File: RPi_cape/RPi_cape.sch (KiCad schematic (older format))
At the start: 108 parts, among them J1 Conn_01x04, J10 Conn_01x02, J11 Conn_01x02, J12 Conn_01x02, J16 Conn_01x06, J2 Conn_01x02, J3 Conn_01x02, J4 Conn_01x02, J5 Conn_01x03, J6 Conn_01x03, J7 Conn_01x02, J8 Conn_02x20_Odd_Even, J9 Conn_01x02, U1 TL431A, U2 ADC128D818, U3 ADC128D818

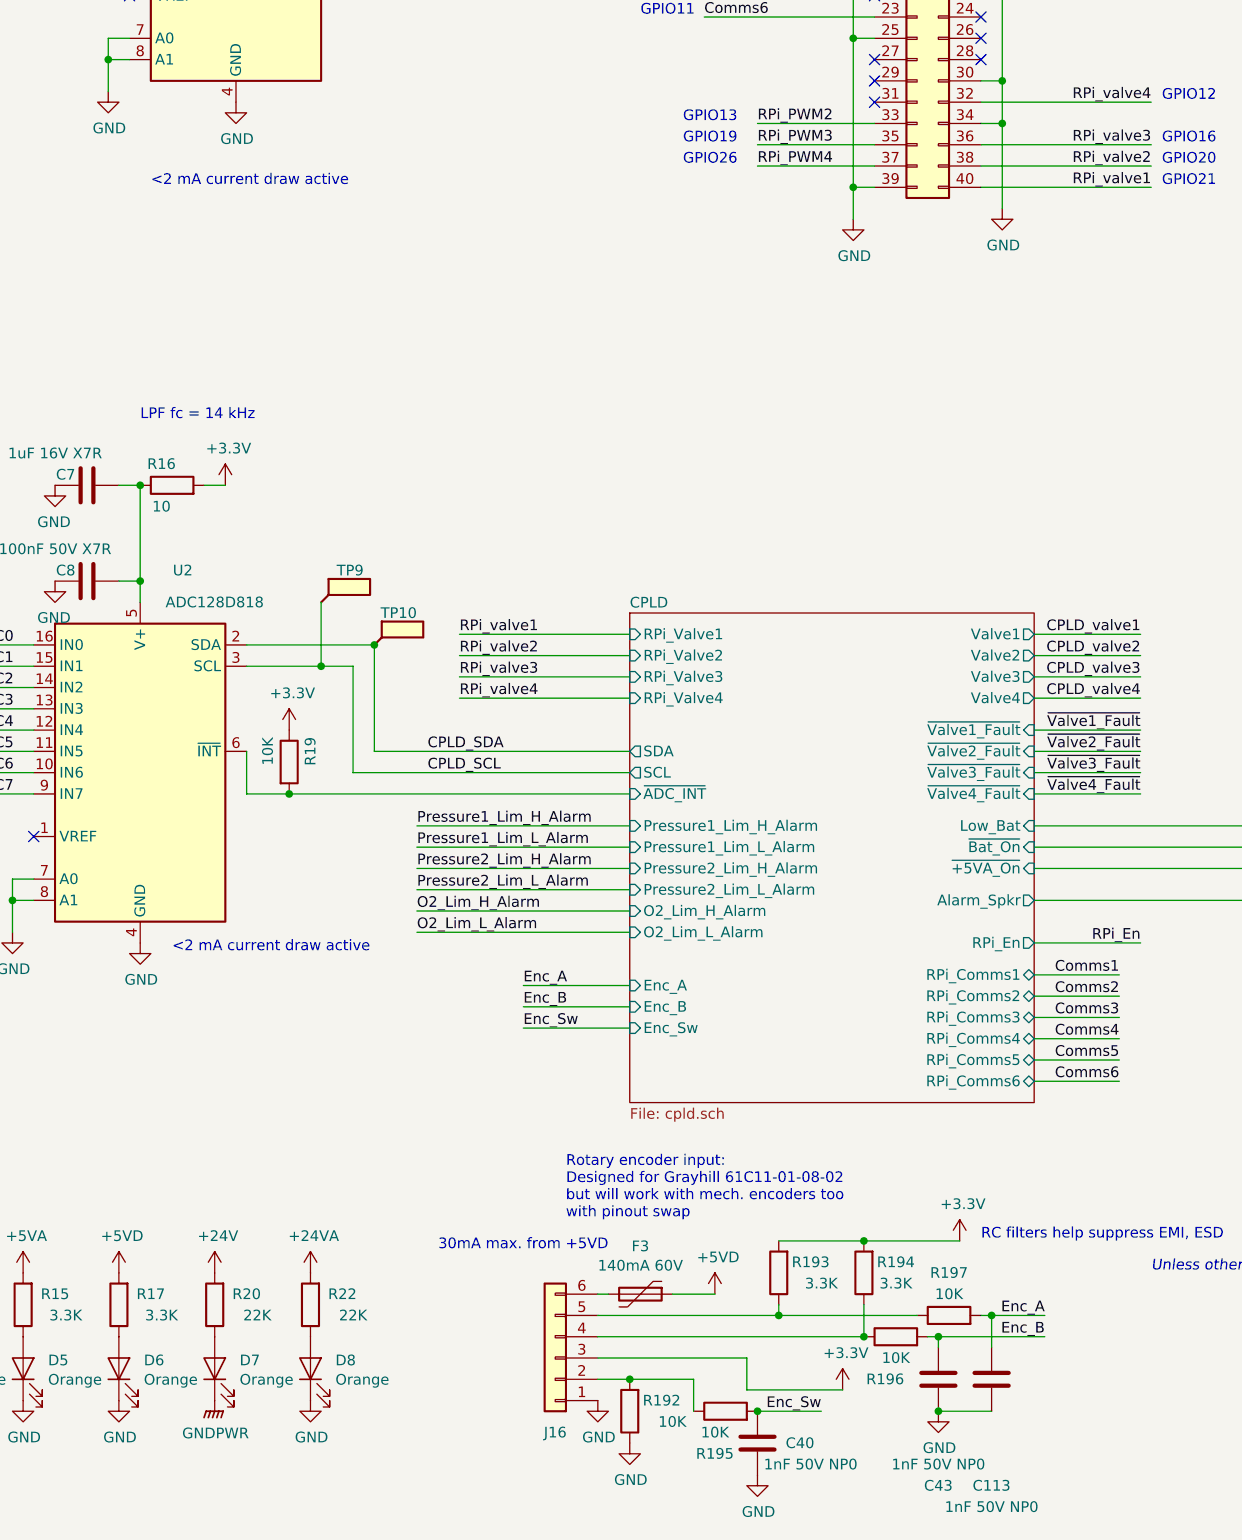
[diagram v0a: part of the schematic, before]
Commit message: Analog upgrades and extra encoder connectors
Renamed a few files
Removed "costing BOM" as difficult to keep up to date, easy to regenerate
Toughened under-voltage detect circuits by adding hysteresis to +5V detect for +BATT diode-OR (R236), filtering to power-down alarm detect input (C85)
Added connector options (J15, J21) for Grayhill C14-series rotary encoder with cable
Changed R190 from 3K to 2.4K to increase overhead on base current required for saturation, and consolidate BOM
Added 3 solderable testpoints for expanding CPLD pin options (TP44-46), adjusted some CPLD pin assignments to allow physical routing to pins
Fixed valve motion detector by changing comparator's hysteresis to AC-only, changing NPN's series resistor to 1K (allows low-enough DC level to count as logic low), and adding optional filtering cap C115 to offset divider
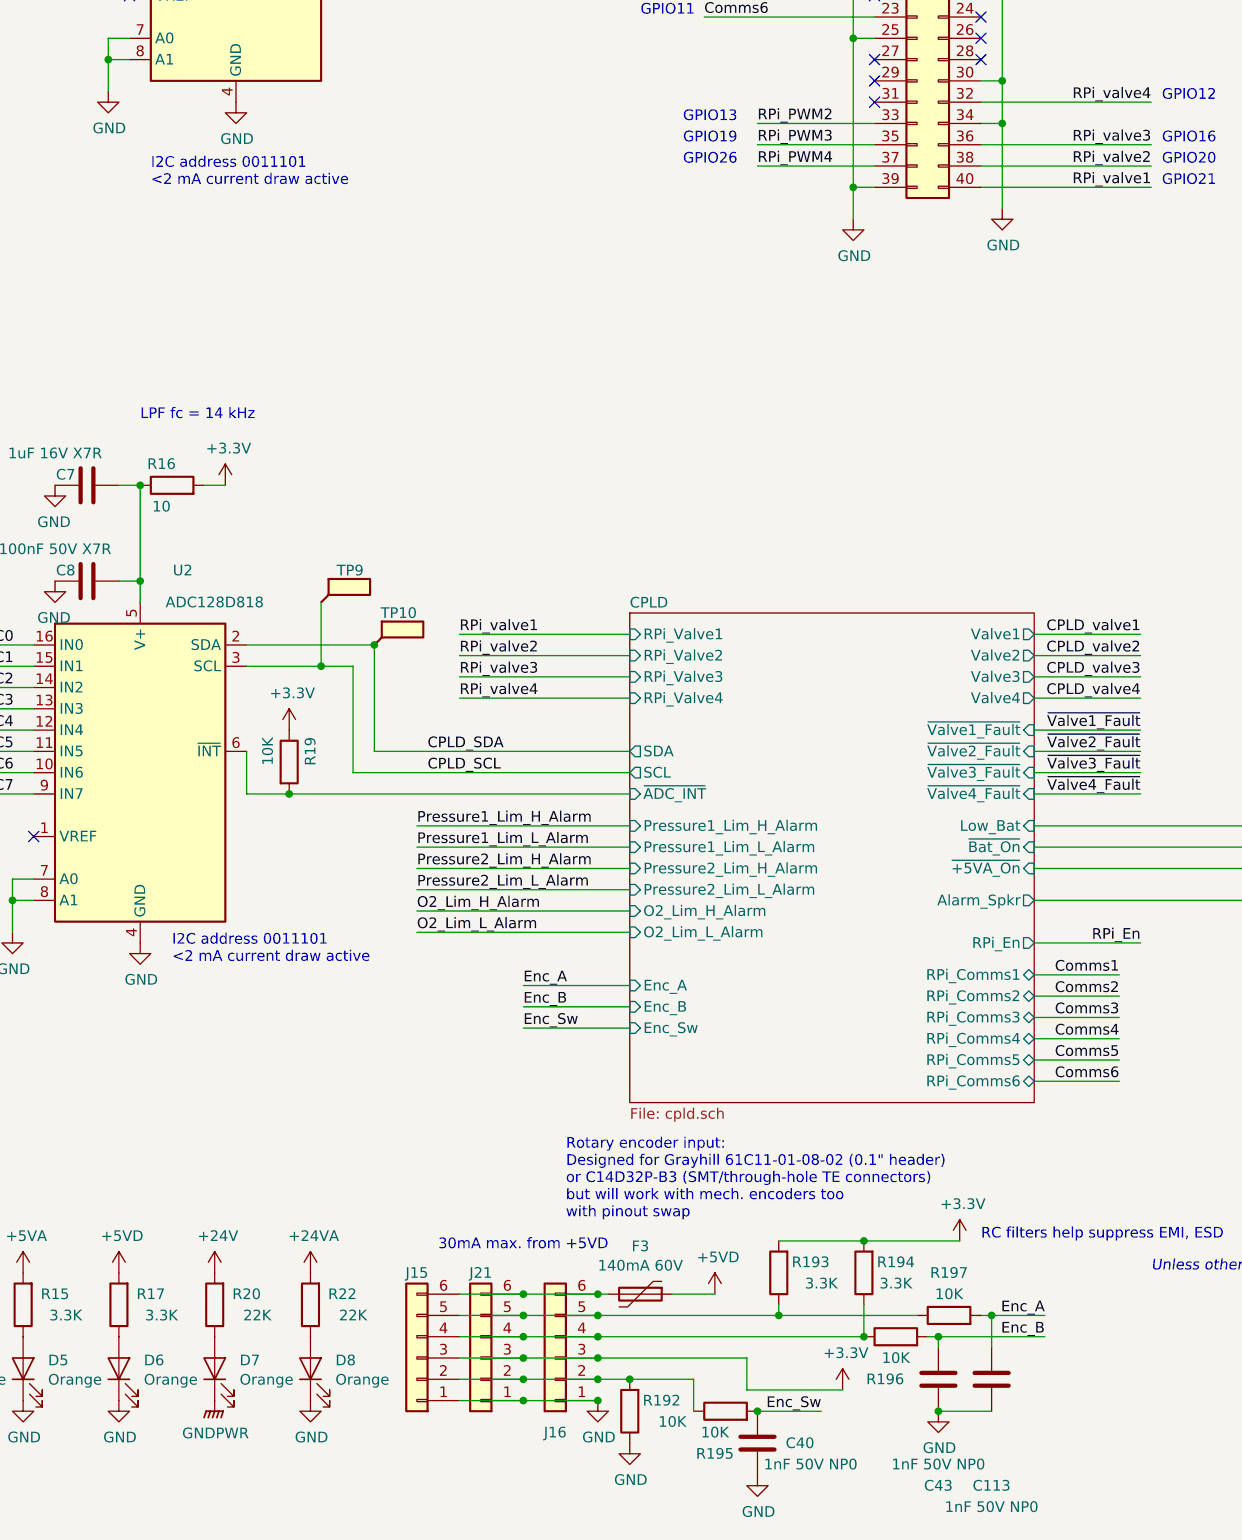
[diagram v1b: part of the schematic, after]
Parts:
- added J15: Conn_01x06, Ventilator:TE_188275-6, symbol Connector_Generic:Conn_01x06
- added J21: Conn_01x06, Ventilator:TE_215079-6, symbol Connector_Generic:Conn_01x06
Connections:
- net +3V3: now also J15.3 (Pin_3), J21.3 (Pin_3)
- net GND: now also J15.1 (Pin_1), J21.1 (Pin_1)
- net at J16.2 (Pin_2), R192.2, R195.1: now also J15.2 (Pin_2), J21.2 (Pin_2)
- net at J16.4 (Pin_4), R194.1, R196.1: now also J15.4 (Pin_4), J21.4 (Pin_4)
- net at J16.5 (Pin_5), R193.1, R197.1: now also J15.5 (Pin_5), J21.5 (Pin_5)
- net at F3.2, J16.6 (Pin_6): now also J15.6 (Pin_6), J21.6 (Pin_6)
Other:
- note added: "I2C address 0011101\n<2 mA current draw active"
- note added: "Rotary encoder input:\nDesigned for Grayhill 61C11-01-08-02 (0.1" header)\nor C14D32P-B3 (SMT/through-hole TE connectors)\nbut will work with mech. encoders too\nwith pinout swap"
- note removed: "<2 mA current draw active"
- note removed: "Rotary encoder input:\nDesigned for Grayhill 61C11-01-08-02\nbut will work with mech. encoders too\nwith pinout swap"
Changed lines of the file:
@@
 Title "Raspberry Pi Hat for JamVent Adaptation"
 Date ""
-Rev "1.7"
+Rev "1.8"
 Comp "US JamVent Team"
 Comment1 "Don Straney"
@@
 $EndComp
 Text Notes 7600 4250 0    50   ~ 0
-<2 mA current draw active
+I2C address 0011101\n<2 mA current draw active
 $Comp
 L power:+5VD #PWR064
@@
 	0    -1   -1   0
 $EndComp
-Text Notes 7700 7850 0    50   ~ 0
-<2 mA current draw active
+Text Notes 7700 7900 0    50   ~ 0
+I2C address 0011101\n<2 mA current draw active
 Wire Wire Line
 	7050 6400 6550 6400
@@
 $EndComp
 Text Notes 9550 9100 0    50   ~ 0
-Rotary encoder input:\nDesigned for Grayhill 61C11-01-08-02\nbut will work with mech. encoders too\nwith pinout swap
+Rotary encoder input:\nDesigned for Grayhill 61C11-01-08-02 (0.1" header)\nor C14D32P-B3 (SMT/through-hole TE connectors)\nbut will work with mech. encoders too\nwith pinout swap
 $Comp
 L power:GND #PWR0140
@@
 Wire Wire Line
 	13350 7700 13850 7700
+$Comp
+L Connector_Generic:Conn_01x06 J21
+U 1 1 5EF6278F
+P 9150 9750
+F 0 "J21" H 9150 9350 50  0000 C CNN
+F 1 "Conn_01x06" H 9068 9316 50  0001 C CNN
+F 2 "Ventilator:TE_215079-6" H 9150 9750 50  0001 C CNN
+F 3 "~" H 9150 9750 50  0001 C CNN
+F 4 "TE AMP" H 9150 9750 50  0001 C CNN "Manufacturer"
+F 5 "215079-6" H 9150 9750 50  0001 C CNN "Part Number"
+	1    9150 9750
+	-1   0    0    1
+$EndComp
+$Comp
+L Connector_Generic:Conn_01x06 J15
+U 1 1 5EF6344E
+P 8850 9750
+F 0 "J15" H 8850 9350 50  0000 C CNN
+F 1 "Conn_01x06" H 8768 9316 50  0001 C CNN
+F 2 "Ventilator:TE_188275-6" H 8850 9750 50  0001 C CNN
+F 3 "~" H 8850 9750 50  0001 C CNN
+F 4 "TE AMP" H 8850 9750 50  0001 C CNN "Manufacturer"
+F 5 "188275-6" H 8850 9750 50  0001 C CNN "Part Number"
+	1    8850 9750
+	-1   0    0    1
+$EndComp
+Wire Wire Line
+	9050 9450 9350 9450
+Connection ~ 9700 9450
+Connection ~ 9350 9450
+Wire Wire Line
+	9350 9450 9700 9450
+Wire Wire Line
+	9050 9550 9350 9550
+Connection ~ 9700 9550
+Connection ~ 9350 9550
+Wire Wire Line
+	9350 9550 9700 9550
+Wire Wire Line
+	9050 9650 9350 9650
+Connection ~ 9700 9650
+Connection ~ 9350 9650
+Wire Wire Line
+	9350 9650 9700 9650
+Wire Wire Line
+	9050 9750 9350 9750
+Connection ~ 9700 9750
+Connection ~ 9350 9750
+Wire Wire Line
+	9350 9750 9700 9750
+Wire Wire Line
+	9050 9850 9350 9850
+Connection ~ 9700 9850
+Connection ~ 9350 9850
+Wire Wire Line
+	9350 9850 9700 9850
+Wire Wire Line
+	9050 9950 9350 9950
+Connection ~ 9700 9950
+Connection ~ 9350 9950
+Wire Wire Line
+	9350 9950 9700 9950
 $EndSCHEMATC
